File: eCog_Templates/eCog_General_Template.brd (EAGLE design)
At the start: 47.5 x 28 mm, 11 parts

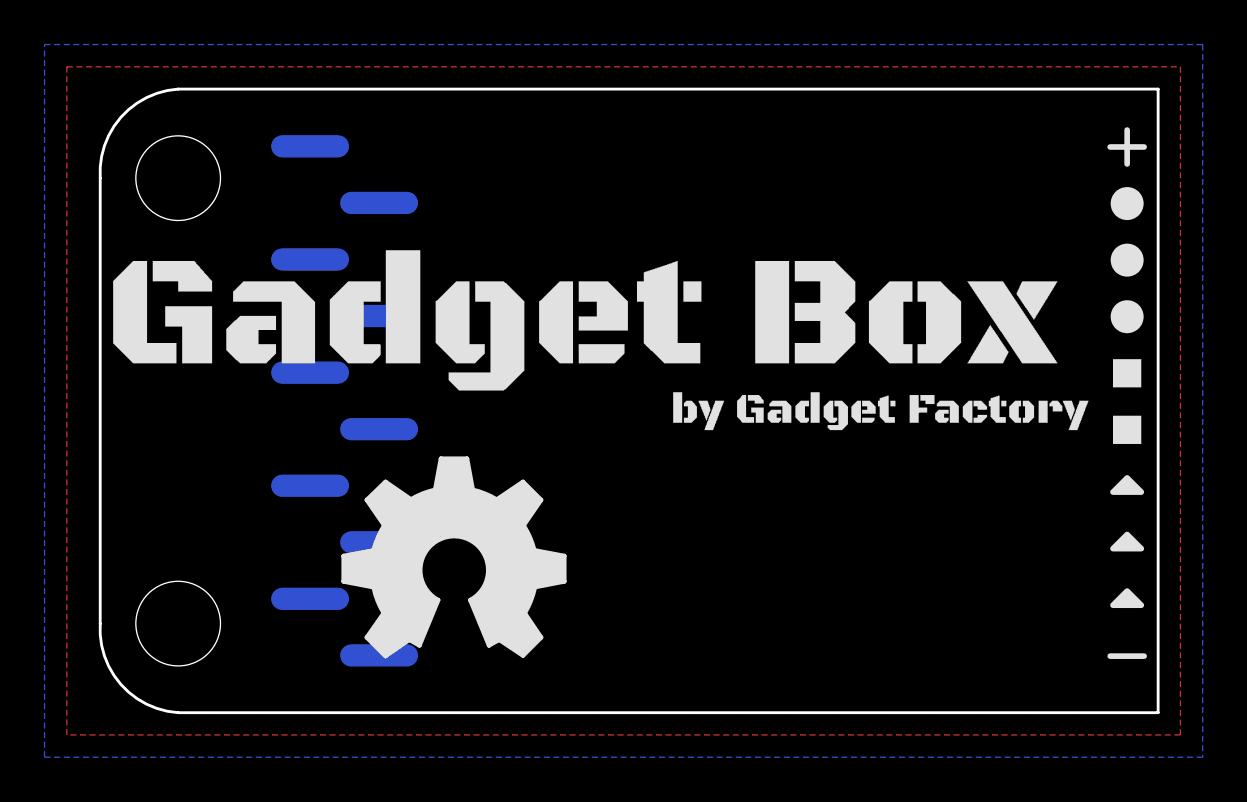
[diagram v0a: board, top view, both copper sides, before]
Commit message: Change to through hole and give bette descriptions.
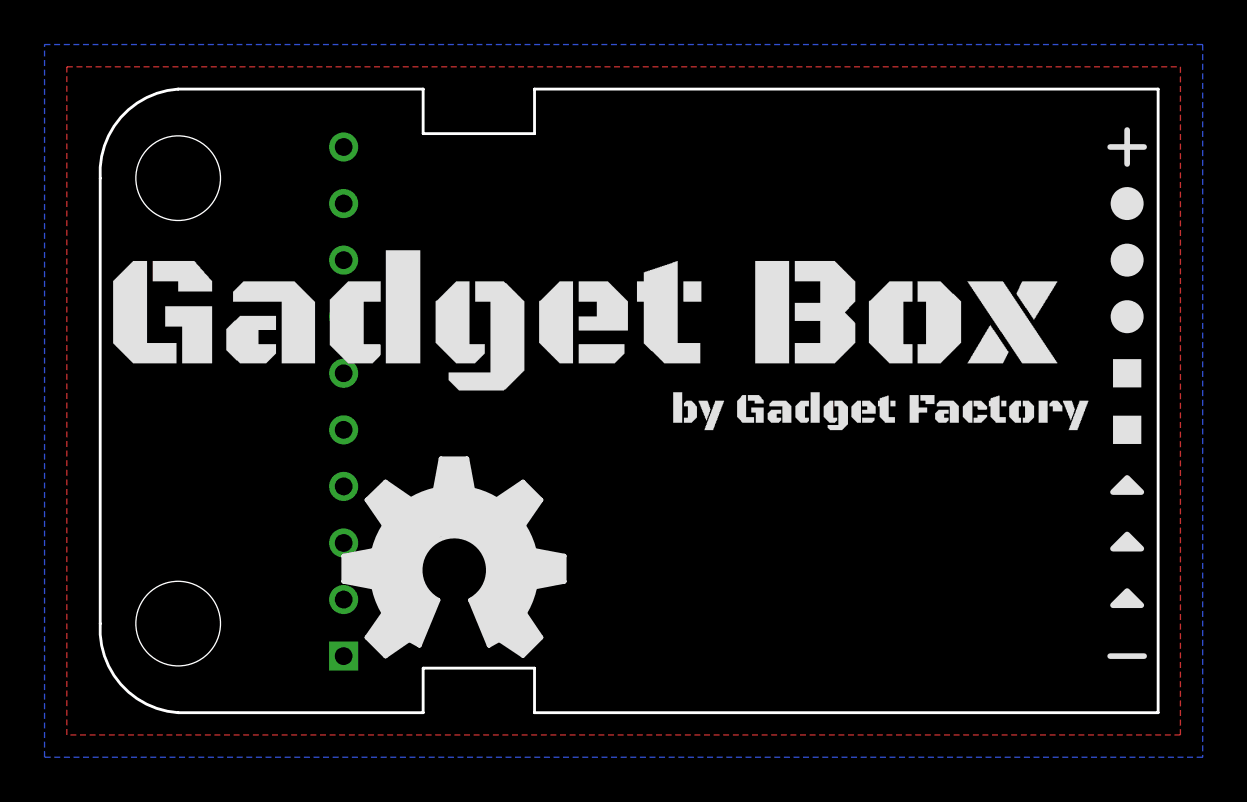
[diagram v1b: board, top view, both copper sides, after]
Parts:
- ECOG: value ECOG_GENERAL_ROWECOG_GENERAL_SMD -> ECOG_GENERAL_ROWTHROUGHOLE; device eCogs:ECOG_GENERAL_SMD -> eCogs:ECOG_GENERAL_TH
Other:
- outline, holes or cut-outs redrawn
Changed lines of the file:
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@@
 </autorouter>
 <elements>
-<element name="ECOG" library="eCogs" package="ECOG_GENERAL_SMD" value="ECOG_GENERAL_ROWECOG_GENERAL_SMD" x="0" y="0" smashed="yes">
-<attribute name="DIGIKEY" value="S1013EC-10-ND" x="0" y="0" size="1.778" layer="27" display="off"/>
-</element>
+<element name="ECOG" library="eCogs" package="ECOG_GENERAL_TH" value="ECOG_GENERAL_ROWTHROUGHOLE" x="0" y="0" smashed="yes"/>
 <element name="U$2" library="eCogs" package="LEGEND_DIO" value="" x="46.609" y="22.86"/>
 <element name="U$3" library="eCogs" package="LEGEND_DIO" value="" x="46.609" y="20.32"/>
